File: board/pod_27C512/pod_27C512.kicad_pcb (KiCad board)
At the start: 2 copper layers, 39.4 x 57.2 mm, 19 parts, among them U1 74HCT02

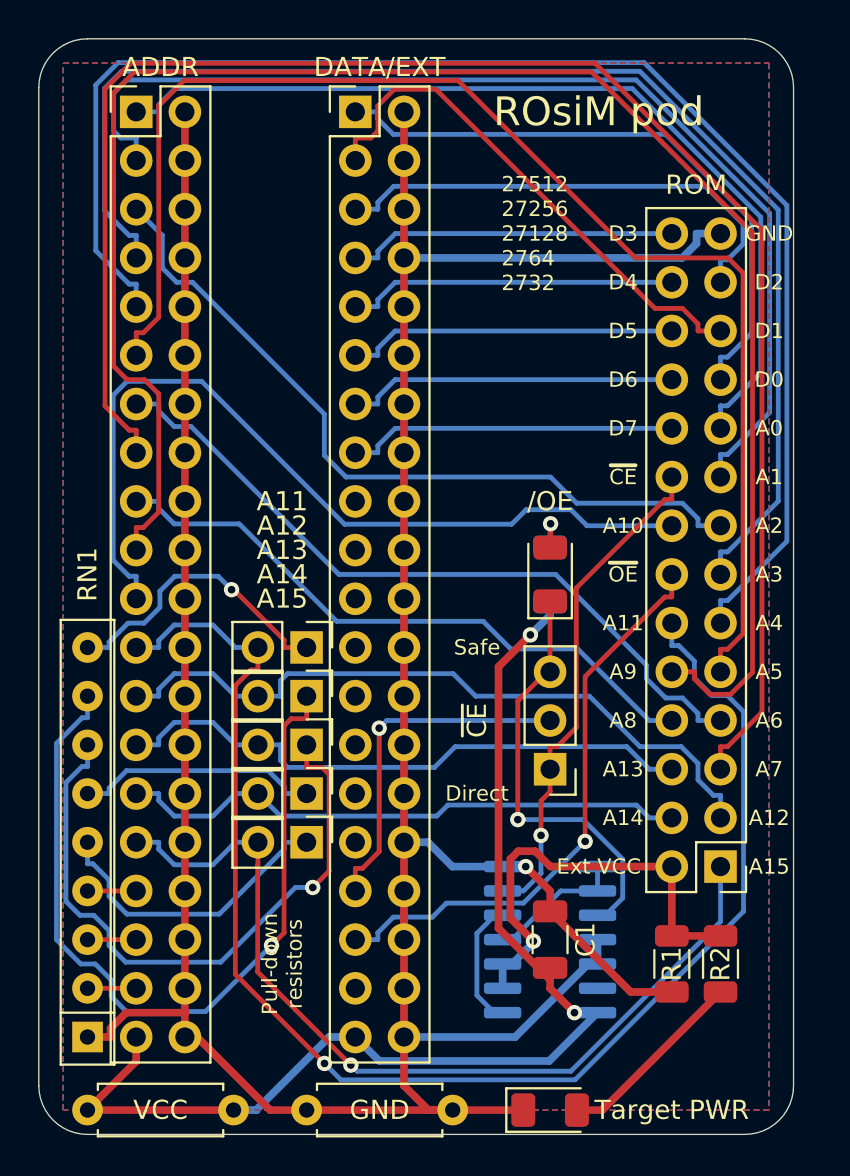
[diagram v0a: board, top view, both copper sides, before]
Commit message: Added pod for 27C400, modified other pods
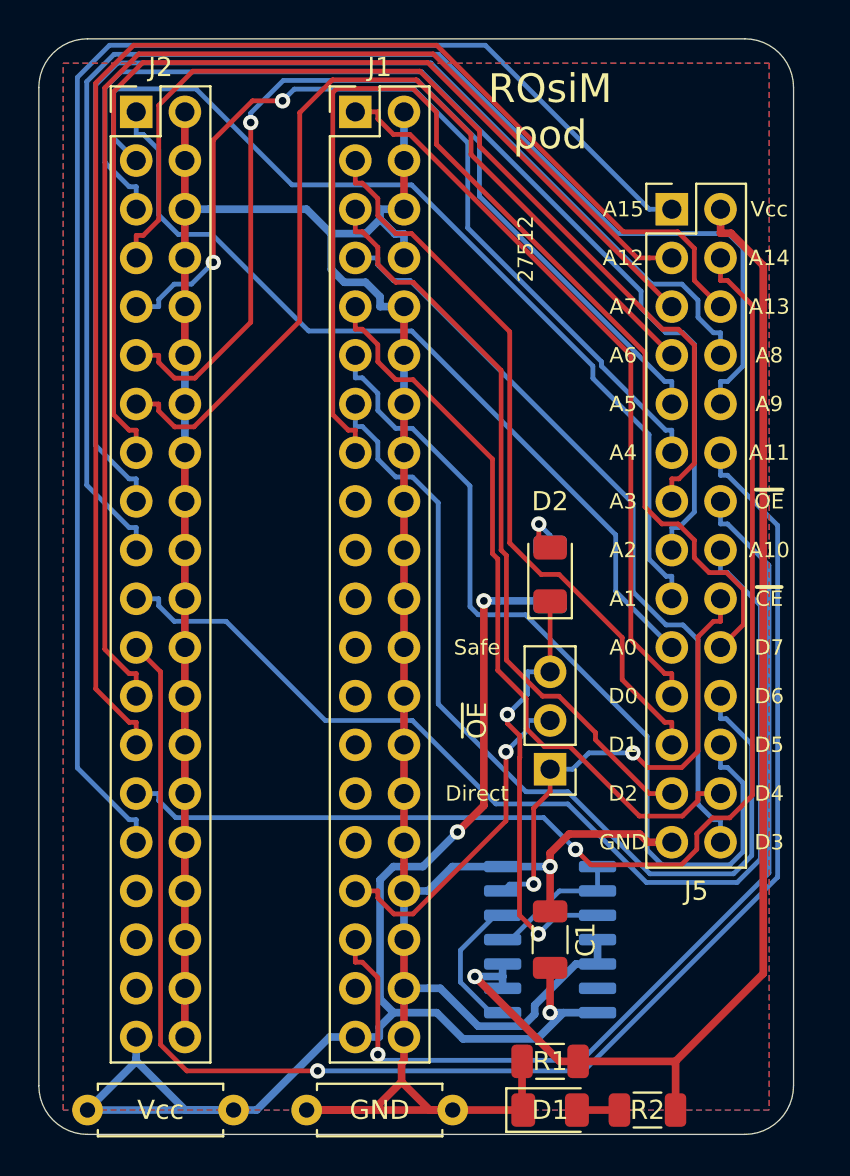
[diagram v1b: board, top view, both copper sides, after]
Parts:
- removed A11, A12, A13, A14, A15: NO, Connector_PinHeader_2.54mm:PinHeader_1x02_P2.54mm_Vertical
- removed RN1: 10k, Resistor_THT:R_Array_SIP9
- D1: renamed from Target PWR
- moved J5 34.4 mm to (162.6, 43.2), turned to 0 degrees
- moved R2 8.52 mm to (161.3, 90.2), turned to 0 degrees
- moved R1 8.13 mm to (156.2, 87.6), turned to 0 degrees
- renumbered /OE to D2, DATA/EXT to J1, ADDR to J2, ROM to J5, VCC to Vcc, ~CE to ~OE
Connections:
- J2 pad 33: /A16 -> (no net)
- J2 pad 35: /A17 -> (no net)
- J2 pad 37: /A18 -> (no net)
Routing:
- net /A13: track 31.0 -> 75.6 mm
- net /D7: track 17.3 -> 61.6 mm
- net Net-(JP3-Pad1): track 42.5 -> 0.00 mm, vias 1 -> 0
- net /EXT_VCC: track 23.3 -> 65.1 mm
- net /A14: track 30.1 -> 64.8 mm, vias 0 -> 1
- net Net-(JP4-Pad1): track 33.8 -> 0.00 mm, vias 1 -> 0
- net /A7: track 87.5 -> 54.6 mm
- net /A8: track 32.9 -> 63.4 mm
- net /D6: track 17.3 -> 47.8 mm
- net /A12: track 36.9 -> 67.3 mm
- net /A15: track 46.7 -> 76.6 mm, vias 1 -> 0
- net /D5: track 17.3 -> 46.2 mm
- net /A4: track 75.7 -> 47.9 mm, vias 0 -> 2
- net /D3: track 17.2 -> 40.3 mm
- net /D4: track 17.3 -> 39.2 mm
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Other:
- board text added: "27512"
- board text added: "Vcc"
- board text removed: "27512 27256 27128 2764 2732"
- board text removed: "Ext VCC"
- board text removed: "Pull-down resistors"

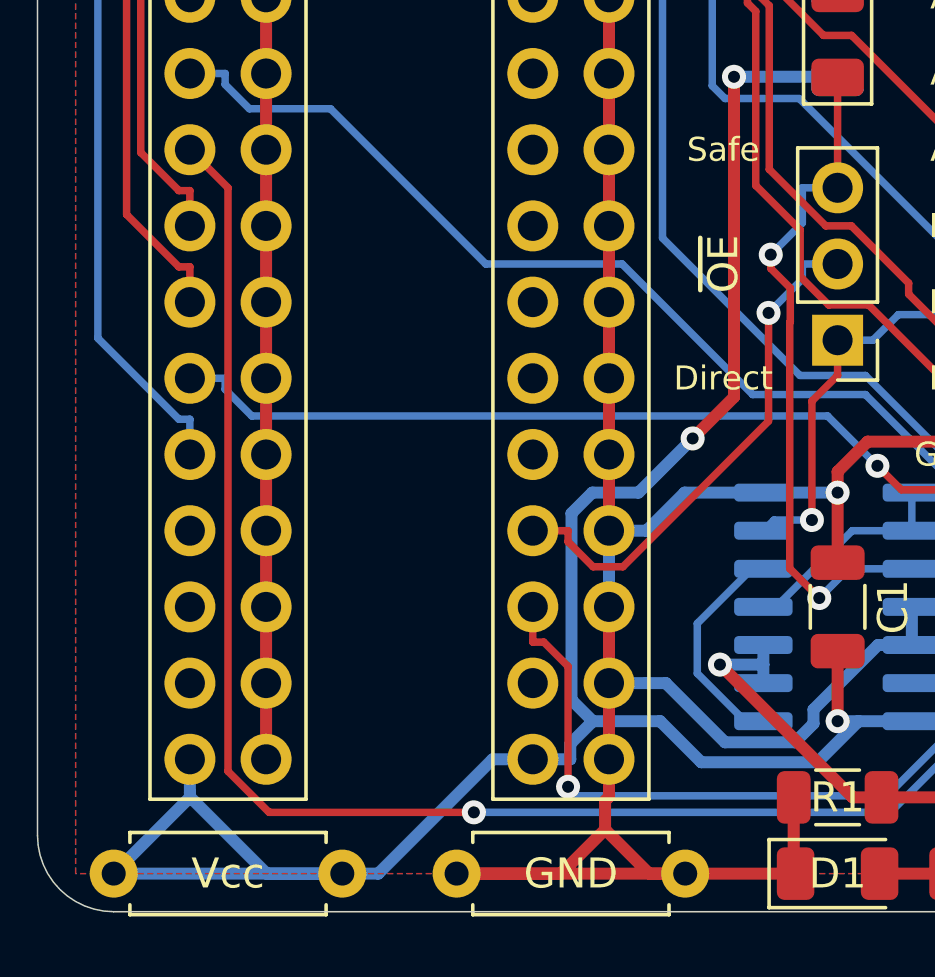
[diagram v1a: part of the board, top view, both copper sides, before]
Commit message: Force unused address lines to low for 27C512 pod
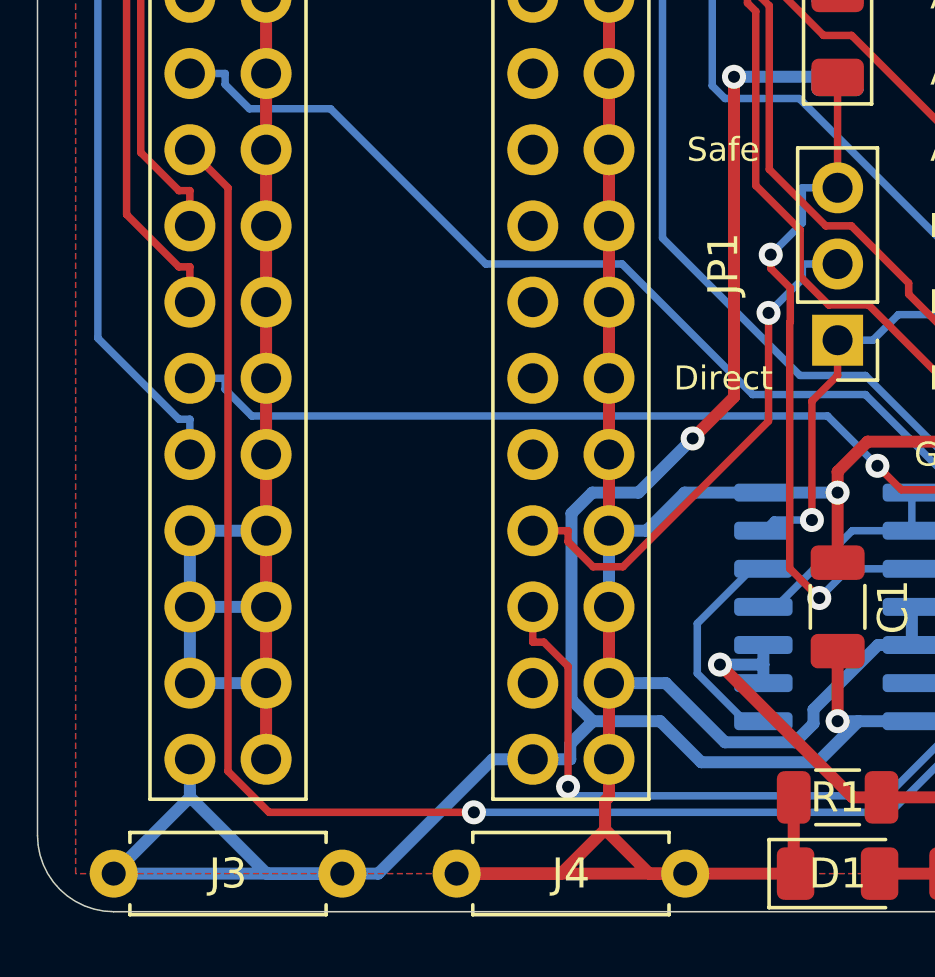
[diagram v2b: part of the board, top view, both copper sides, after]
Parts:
- renumbered Vcc to J3, GND to J4, ~OE to JP1
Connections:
- J2 pad 33: (no net) -> GND
- J2 pad 35: (no net) -> GND
- J2 pad 37: (no net) -> GND
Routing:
- net GND: track 170.8 -> 183.5 mm
